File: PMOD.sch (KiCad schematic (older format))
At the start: 3 parts, among them J12 Conn_02x06_Odd_Even, J13 Conn_02x06_Odd_Even, J16 Conn_02x06_Odd_Even

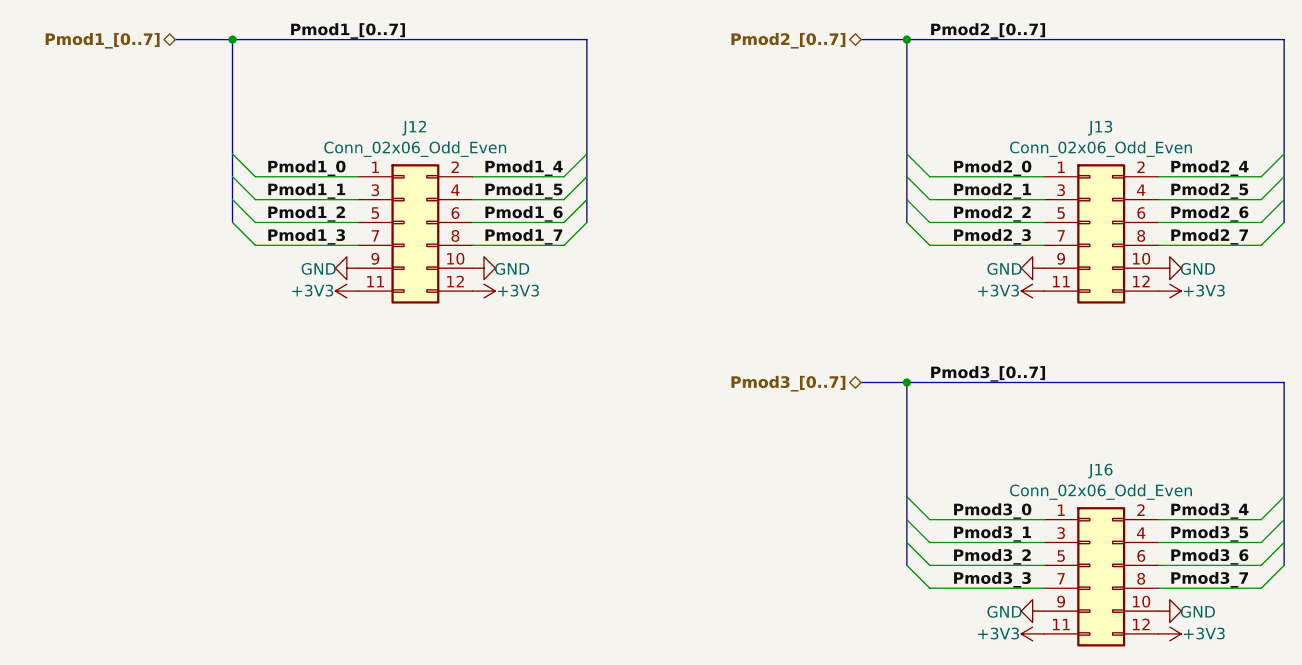
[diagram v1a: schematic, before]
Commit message: BOM configuration file edited, updated Marble picture, some components part number changed
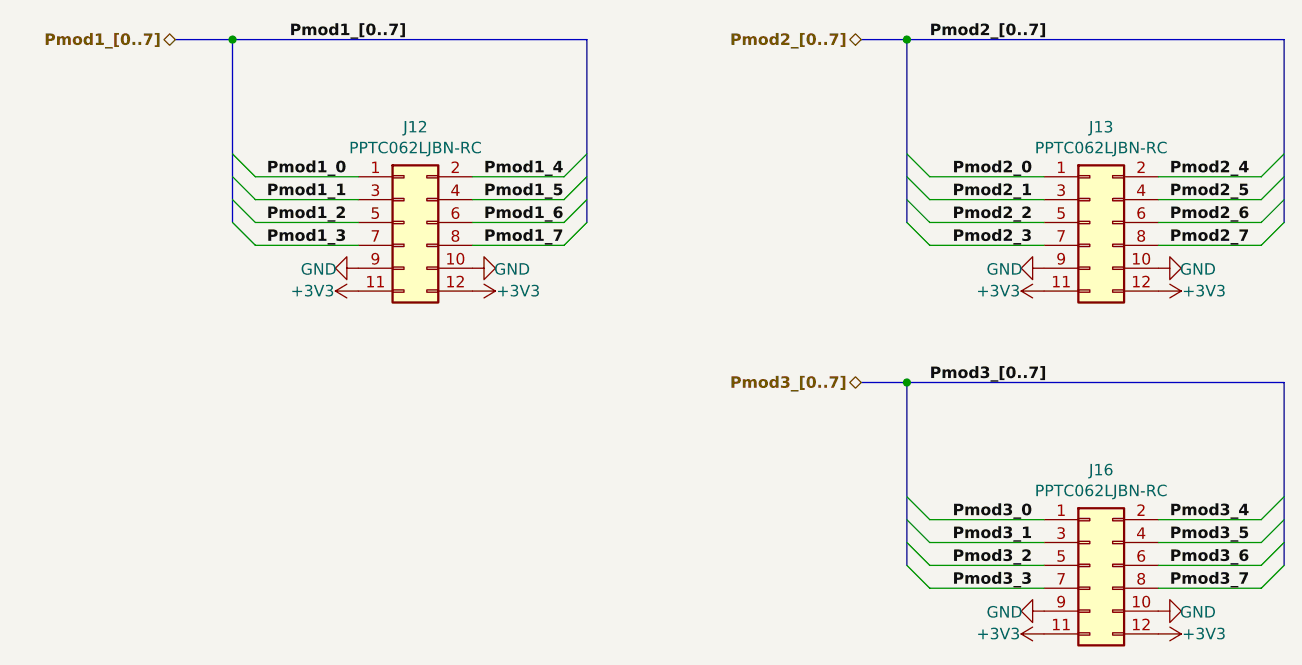
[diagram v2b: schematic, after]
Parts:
- J12, J13, J16: value Conn_02x06_Odd_Even -> PPTC062LJBN-RC; Manufacturer Part Number (none) -> PPTC062LJBN-RC
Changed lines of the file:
@@
 P 3750 2900
 F 0 "J12" H 3800 3317 50  0000 C CNN
-F 1 "Conn_02x06_Odd_Even" H 3800 3226 50  0000 C CNN
+F 1 "PPTC062LJBN-RC" H 3800 3226 50  0000 C CNN
 F 2 "Connectors_Samtec:SDL-112-X-XX_2x06" H 3750 2900 50  0001 C CNN
 F 3 "~" H 3750 2900 50  0001 C CNN
+F 4 "PPTC062LJBN-RC" H 3750 2900 50  0001 C CNN "Manufacturer Part Number"
 	1    3750 2900
 	1    0    0    -1
@@
 P 6750 2900
 F 0 "J13" H 6800 3317 50  0000 C CNN
-F 1 "Conn_02x06_Odd_Even" H 6800 3226 50  0000 C CNN
+F 1 "PPTC062LJBN-RC" H 6800 3226 50  0000 C CNN
 F 2 "Connectors_Samtec:SDL-112-X-XX_2x06" H 6750 2900 50  0001 C CNN
 F 3 "~" H 6750 2900 50  0001 C CNN
+F 4 "PPTC062LJBN-RC" H 6750 2900 50  0001 C CNN "Manufacturer Part Number"
 	1    6750 2900
 	1    0    0    -1
@@
 P 6750 4400
 F 0 "J16" H 6800 4817 50  0000 C CNN
-F 1 "Conn_02x06_Odd_Even" H 6800 4726 50  0000 C CNN
+F 1 "PPTC062LJBN-RC" H 6800 4726 50  0000 C CNN
 F 2 "Connectors_Samtec:SDL-112-X-XX_2x06" H 6750 4400 50  0001 C CNN
 F 3 "~" H 6750 4400 50  0001 C CNN
+F 4 "PPTC062LJBN-RC" H 6750 4400 50  0001 C CNN "Manufacturer Part Number"
 	1    6750 4400
 	1    0    0    -1

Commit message: Configure three Pmod connectors as dnf for AMC builds
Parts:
- J12, J13, J16: config (none) -> +standalone
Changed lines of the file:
@@
 F 3 "~" H 3750 2900 50  0001 C CNN
 F 4 "PPTC062LJBN-RC" H 3750 2900 50  0001 C CNN "Manufacturer Part Number"
+F 5 "+standalone" H 3750 2900 50  0001 C CNN "config"
 	1    3750 2900
 	1    0    0    -1
@@
 F 3 "~" H 6750 2900 50  0001 C CNN
 F 4 "PPTC062LJBN-RC" H 6750 2900 50  0001 C CNN "Manufacturer Part Number"
+F 5 "+standalone" H 6750 2900 50  0001 C CNN "config"
 	1    6750 2900
 	1    0    0    -1
@@
 F 3 "~" H 6750 4400 50  0001 C CNN
 F 4 "PPTC062LJBN-RC" H 6750 4400 50  0001 C CNN "Manufacturer Part Number"
+F 5 "+standalone" H 6750 4400 50  0001 C CNN "config"
 	1    6750 4400
 	1    0    0    -1

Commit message: Convert all footprints to use Marble nickname
Includes both .sch and .lib files
Includes both bare footprint names and those with CERN-like nicknames
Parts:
- J12, J13, J16: footprint Connectors_Samtec:SDL-112-X-XX_2x06 -> Marble:SDL-112-X-XX_2x06
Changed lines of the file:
@@
 F 0 "J12" H 3800 3317 50  0000 C CNN
 F 1 "PPTC062LJBN-RC" H 3800 3226 50  0000 C CNN
-F 2 "Connectors_Samtec:SDL-112-X-XX_2x06" H 3750 2900 50  0001 C CNN
+F 2 "Marble:SDL-112-X-XX_2x06" H 3750 2900 50  0001 C CNN
 F 3 "~" H 3750 2900 50  0001 C CNN
 F 4 "PPTC062LJBN-RC" H 3750 2900 50  0001 C CNN "Manufacturer Part Number"
@@
 F 0 "J13" H 6800 3317 50  0000 C CNN
 F 1 "PPTC062LJBN-RC" H 6800 3226 50  0000 C CNN
-F 2 "Connectors_Samtec:SDL-112-X-XX_2x06" H 6750 2900 50  0001 C CNN
+F 2 "Marble:SDL-112-X-XX_2x06" H 6750 2900 50  0001 C CNN
 F 3 "~" H 6750 2900 50  0001 C CNN
 F 4 "PPTC062LJBN-RC" H 6750 2900 50  0001 C CNN "Manufacturer Part Number"
@@
 F 0 "J16" H 6800 4817 50  0000 C CNN
 F 1 "PPTC062LJBN-RC" H 6800 4726 50  0000 C CNN
-F 2 "Connectors_Samtec:SDL-112-X-XX_2x06" H 6750 4400 50  0001 C CNN
+F 2 "Marble:SDL-112-X-XX_2x06" H 6750 4400 50  0001 C CNN
 F 3 "~" H 6750 4400 50  0001 C CNN
 F 4 "PPTC062LJBN-RC" H 6750 4400 50  0001 C CNN "Manufacturer Part Number"

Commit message: List more Manufacturers
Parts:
- J12, J13, J16: Manufacturer (none) -> SULLINS
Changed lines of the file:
@@
 F 4 "PPTC062LJBN-RC" H 3750 2900 50  0001 C CNN "Manufacturer Part Number"
 F 5 "+standalone" H 3750 2900 50  0001 C CNN "config"
+F 6 "SULLINS" H 3750 2900 50  0001 C CNN "Manufacturer"
 	1    3750 2900
 	1    0    0    -1
@@
 F 4 "PPTC062LJBN-RC" H 6750 2900 50  0001 C CNN "Manufacturer Part Number"
 F 5 "+standalone" H 6750 2900 50  0001 C CNN "config"
+F 6 "SULLINS" H 6750 2900 50  0001 C CNN "Manufacturer"
 	1    6750 2900
 	1    0    0    -1
@@
 F 4 "PPTC062LJBN-RC" H 6750 4400 50  0001 C CNN "Manufacturer Part Number"
 F 5 "+standalone" H 6750 4400 50  0001 C CNN "config"
+F 6 "SULLINS" H 6750 4400 50  0001 C CNN "Manufacturer"
 	1    6750 4400
 	1    0    0    -1
